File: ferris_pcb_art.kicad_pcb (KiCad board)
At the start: 2 copper layers, 30 x 30 mm, 1 part

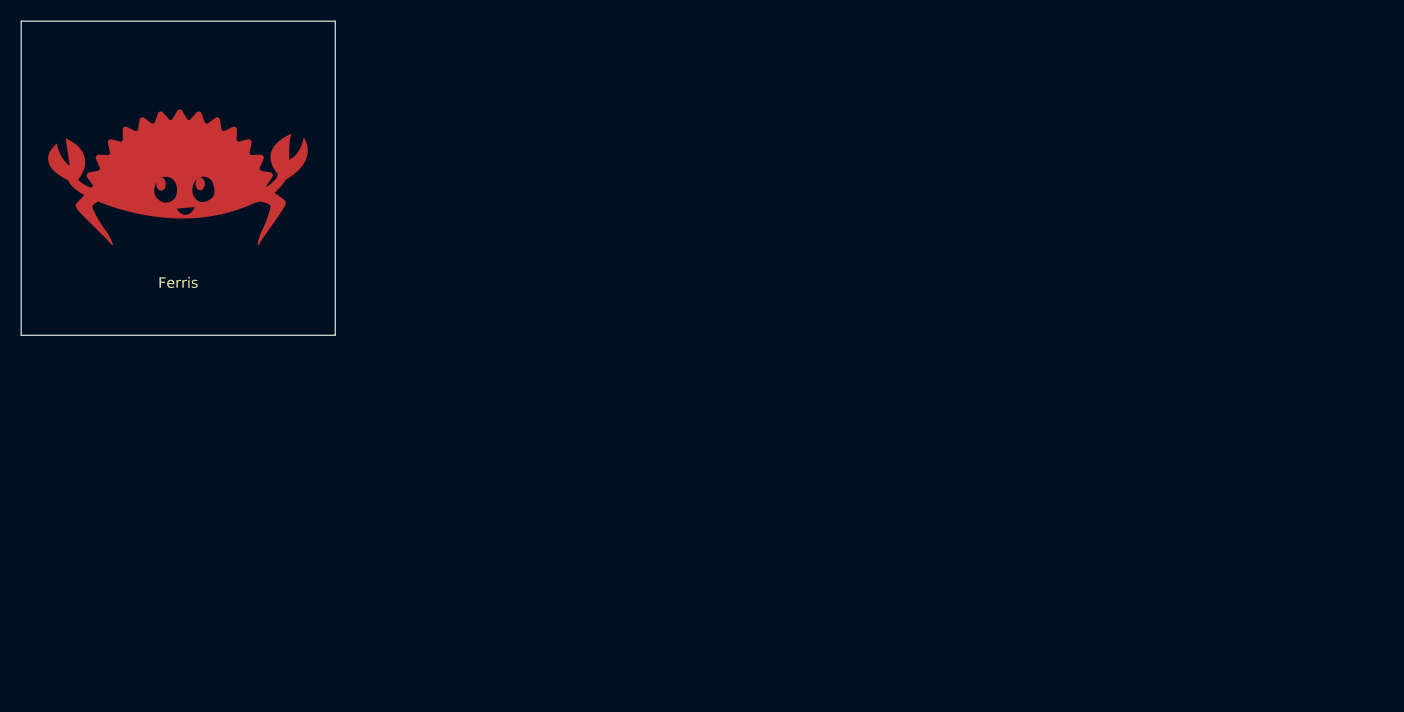
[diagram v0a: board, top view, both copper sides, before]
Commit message: Add all the copper pads I've made so far
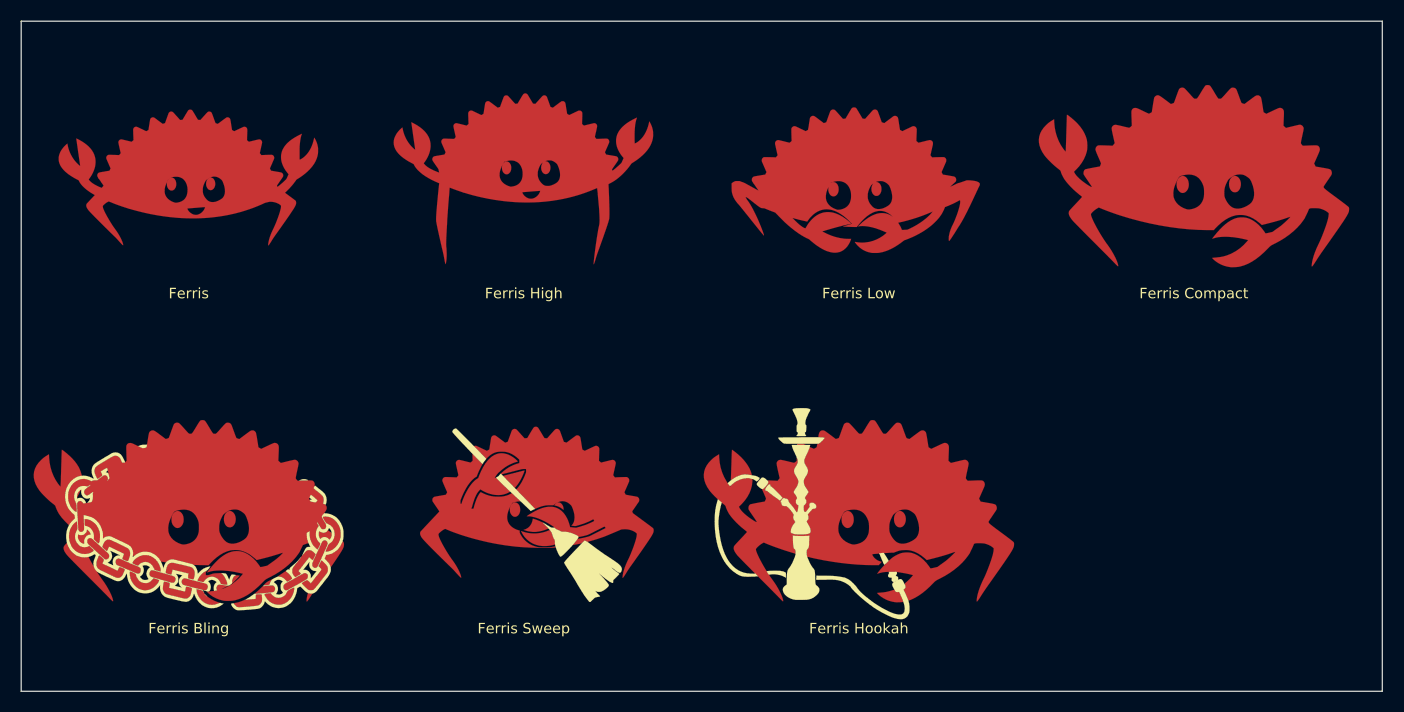
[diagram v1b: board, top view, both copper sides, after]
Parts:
- added G***: LOGO, copper_pads:ferris_hookah, F.Cu at (92.0, 59.0)
- added G***: LOGO, copper_pads:ferris_sweep, F.Cu at (60.0, 59.0)
- added G***: LOGO, copper_pads:ferris_bling, F.Cu at (28.0, 59.0)
- added G***: LOGO, copper_pads:ferris_compact, F.Cu at (124.0, 27.0)
- added G***: LOGO, copper_pads:ferris_low, F.Cu at (92.0, 27.0)
- added G***: LOGO, copper_pads:ferris_high, F.Cu at (60.0, 27.0)
- moved G*** 1.00 mm to (28.0, 27.0)
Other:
- board size 30 x 30 mm -> 130 x 64 mm
- board text added: "Ferris Bling"
- board text added: "Ferris Compact"
- board text added: "Ferris High"
- board text added: "Ferris Hookah"
- board text added: "Ferris Low"
- board text added: "Ferris Sweep"
